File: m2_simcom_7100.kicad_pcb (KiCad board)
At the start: 2 copper layers, 42 x 30 mm, 5 parts, among them J1 M.2_Key_B

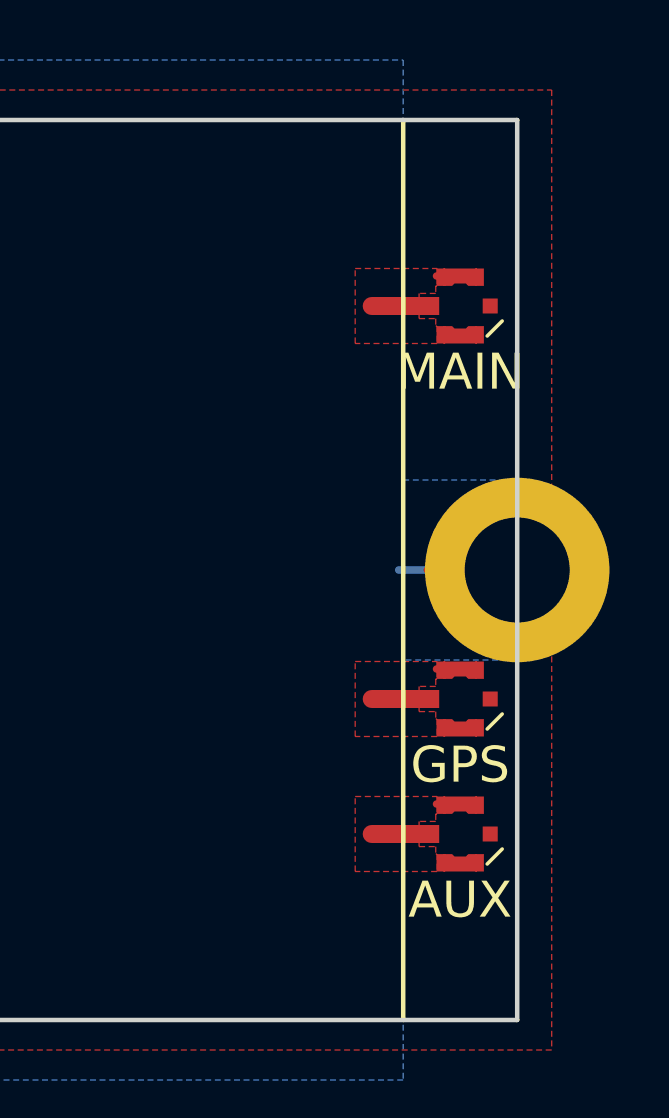
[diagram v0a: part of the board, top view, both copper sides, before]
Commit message: Fix footprint associations in netlist which are pointing to the wrong library name
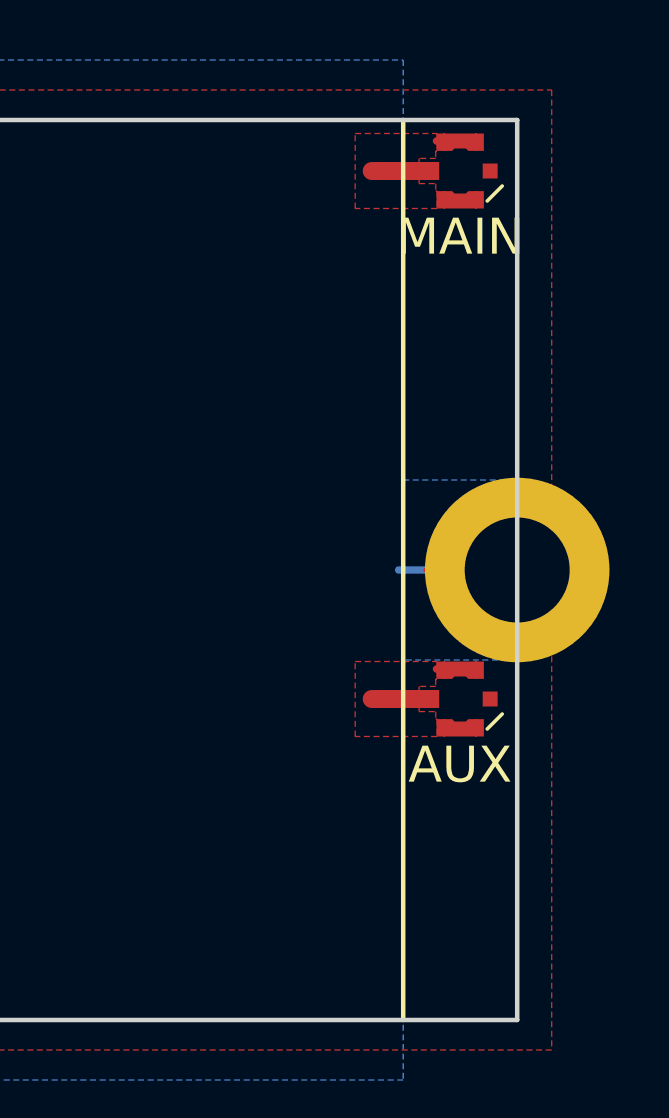
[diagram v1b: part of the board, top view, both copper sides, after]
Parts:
- removed ANT1: Conn_Coaxial, m2_key_b_3042:MHF4_20449-001E
- ANT2: footprint m2_key_b_3042:MHF4_20449-001E -> m2_simcom_7100:MHF4_20449-001E
- ANT5: renamed from ANT4; footprint m2_key_b_3042:MHF4_20449-001E -> m2_simcom_7100:MHF4_20449-001E
- J1: footprint m2_key_b_3042:M.2_Key_B_Gold_Fingers -> m2_simcom_7100:M.2_Key_B_Gold_Fingers
- moved ANT5 4.50 mm to (158.9, 81.7)
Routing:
- net /AUX: track 1.97 -> 0.00 mm
- net GND: track 31.9 -> 31.1 mm
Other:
- board text removed: "GPS"

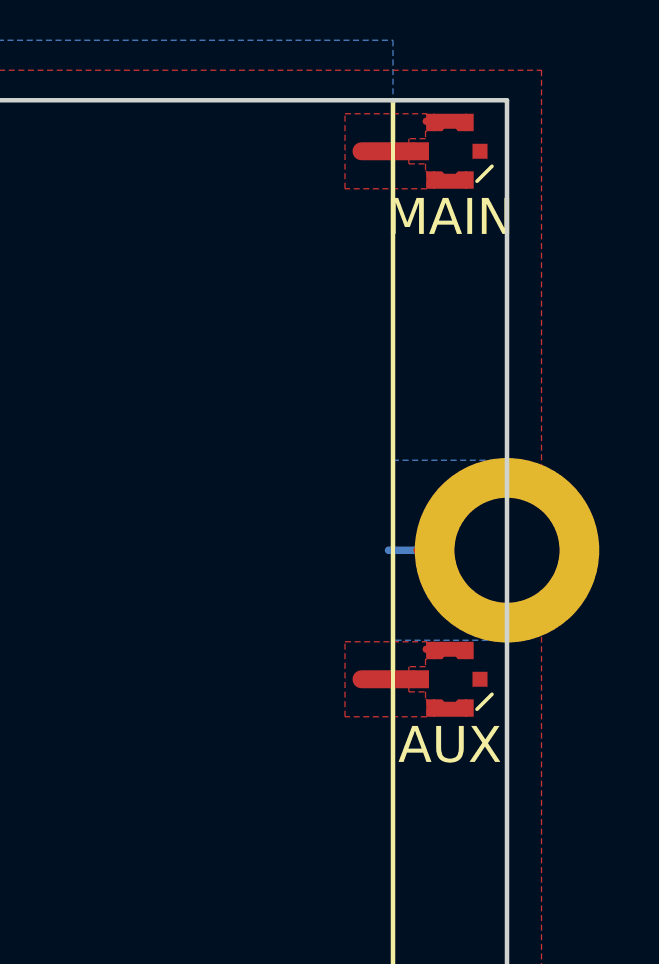
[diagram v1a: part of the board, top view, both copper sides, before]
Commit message: Swap Main and Div antenna positions
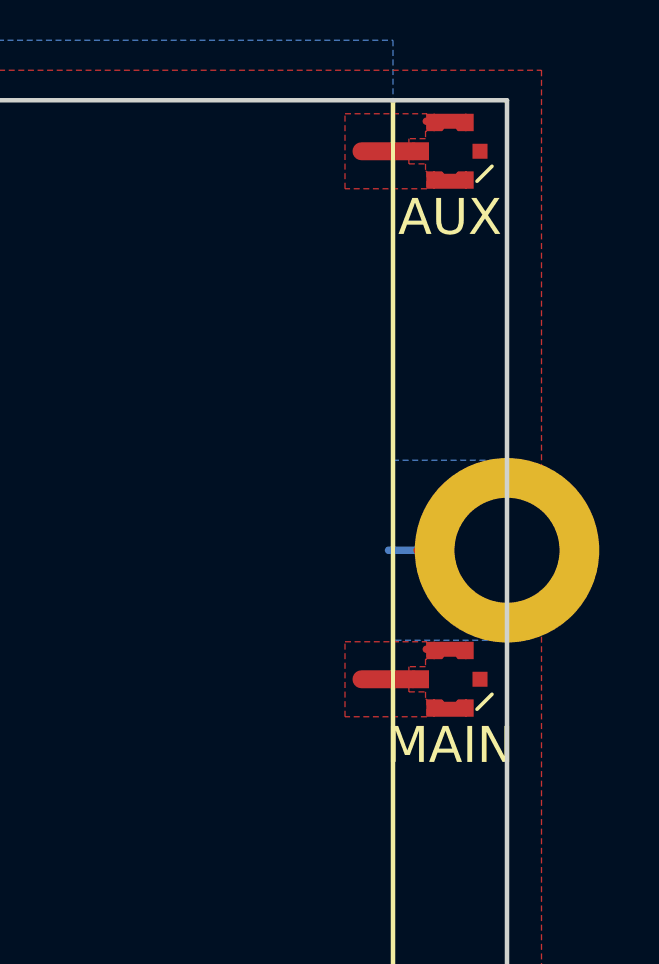
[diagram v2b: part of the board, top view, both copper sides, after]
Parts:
- ANT2: value Conn_Coaxial -> Main_Antenna
- ANT5: value Conn_Coaxial -> Div_Antenna
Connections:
- net +3V3 renamed VBAT
- net /DEVSLP renamed Net-(J1-Pad38)
- net /GPIO_0 renamed /HSIC_Data
- net /GPIO_1 renamed /HSIC_Strobe
- net /GPIO_10 renamed /UART_CTS
- net /GPIO_11 renamed /UART_RI/~WoWWAN
- net /GPIO_12 renamed /UART_RX
- net /GPIO_2 renamed /UART_DTR
- net /GPIO_3 renamed /UART_RTS
- net /GPIO_4 renamed /UART_DCD
- net /GPIO_5 renamed /PCM_CLK
- net /GPIO_6 renamed /PCM_IN
- net /GPIO_7 renamed /PCM_OUT
- net /GPIO_8 renamed /PCM_SYNC
- net /GPIO_9/DAS/~DSS renamed /UART_TX
- net /GPS renamed Net-(ANT2-Pad1)
- net /MAIN renamed Net-(ANT5-Pad1)
- net /PERn0/SATA-B+ renamed Net-(J1-Pad41)
- net /PERn1/USB3.0-Rx-/SSIC-RxN renamed /USB3.0-Tx-
- net /PERp0/SATA-B- renamed Net-(J1-Pad43)
- net /PERp1/USB3.0-Rx+/SSIC-RxP renamed /USB3.0-Tx+
- net /PETn0/SATA-A- renamed Net-(J1-Pad47)
- net /PETn1/USB3.0-Tx-/SSIC-TxN renamed /USB3.0-Rx-
- net /PETp0/SATA-A+ renamed Net-(J1-Pad49)
- net /PETp1/USB3.0-Tx+/SSIC-TxP renamed /USB3.0-Rx+
- net /REFCLKN renamed Net-(J1-Pad53)
- net /REFCLKP renamed Net-(J1-Pad55)
- net /~CLKREQ renamed Net-(J1-Pad52)
- net /~PERST renamed Net-(J1-Pad50)
- net /~PEWake renamed Net-(J1-Pad54)
- J1 pad 21: /CONFIG_0 -> GND

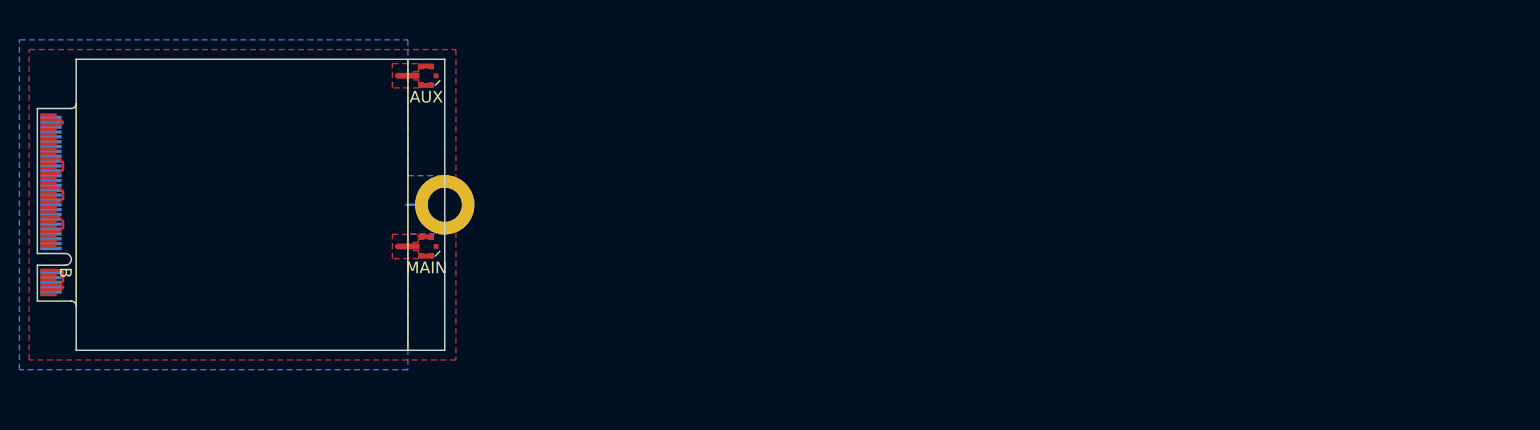
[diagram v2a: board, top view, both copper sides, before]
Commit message: Import the netlist and associated footprints into the layout
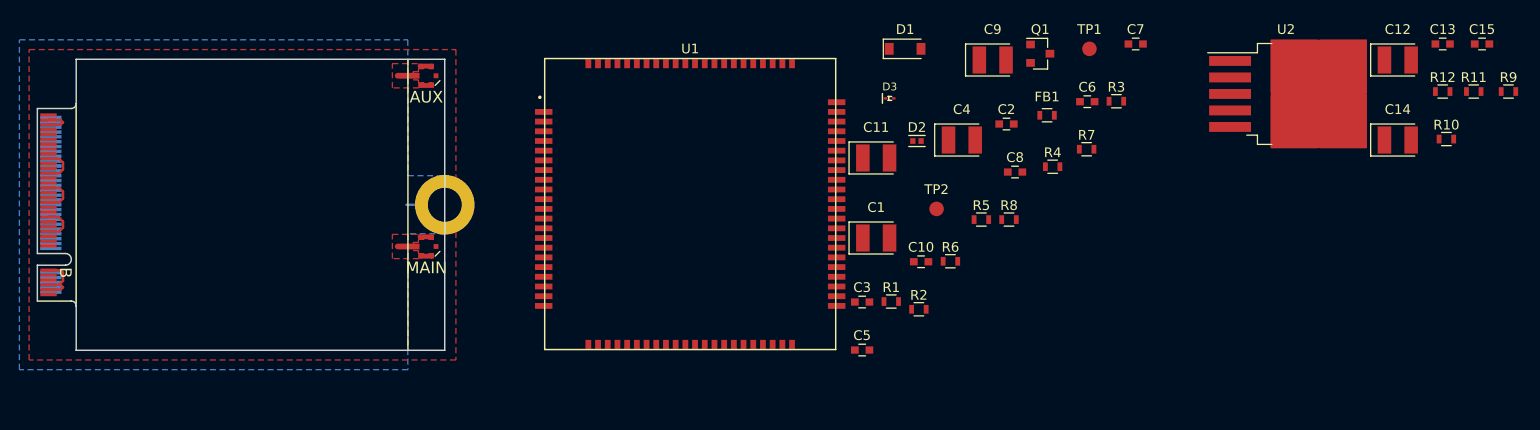
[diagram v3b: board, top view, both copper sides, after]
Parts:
- added C1: 100uF, m2_simcom_7100:CP_Tantalum_Case-B_EIA-3528-21_Reflow, F.Cu at (205.3, 98.4)
- added C10: NC, Capacitors_SMD:C_0603, F.Cu at (210.0, 100.9)
- added C11: 100uF, m2_simcom_7100:CP_Tantalum_Case-B_EIA-3528-21_Reflow, F.Cu at (205.3, 90.2)
- added C12: 100uF, m2_simcom_7100:CP_Tantalum_Case-B_EIA-3528-21_Reflow, F.Cu at (259.1, 80.1)
- added C13: 1uF, Capacitors_SMD:C_0603, F.Cu at (263.7, 78.4)
- added C14: 100uF, m2_simcom_7100:CP_Tantalum_Case-B_EIA-3528-21_Reflow, F.Cu at (259.1, 88.3)
- added C15: 100nF, Capacitors_SMD:C_0603, F.Cu at (267.8, 78.4)
- added C2: NC, Capacitors_SMD:C_0603, F.Cu at (218.8, 86.7)
- added C3: NC, Capacitors_SMD:C_0603, F.Cu at (203.9, 105.0)
- added C4: NC, m2_simcom_7100:CP_Tantalum_Case-B_EIA-3528-21_Reflow, F.Cu at (214.2, 88.3)
- added C5: 1uF, Capacitors_SMD:C_0603, F.Cu at (203.9, 110.0)
- added C6: NC, Capacitors_SMD:C_0603, F.Cu at (227.1, 84.4)
- added C7: NC, Capacitors_SMD:C_0603, F.Cu at (232.1, 78.4)
- added C8: 100nF, Capacitors_SMD:C_0603, F.Cu at (219.6, 91.6)
- added C9: 100uF, m2_simcom_7100:CP_Tantalum_Case-B_EIA-3528-21_Reflow, F.Cu at (217.3, 80.1)
- added D1: MMSZ5231BT1G, m2_simcom_7100:D_SOD-123, F.Cu at (208.3, 78.9)
- added D2: NC, m2_simcom_7100:D_0402, F.Cu at (209.5, 88.4)
- added D3: ESD9L5.0ST5G, m2_simcom_7100:D_SOD-923, F.Cu at (206.7, 84.0)
- added FB1: Ferrite, Inductors_SMD:L_0603, F.Cu at (222.9, 85.8)
- added Q1: NC, TO_SOT_Packages_SMD:SOT-23, F.Cu at (222.2, 79.4)
- added R1: NC, Resistors_SMD:R_0603, F.Cu at (206.9, 105.0)
- added R10: 100k, Resistors_SMD:R_0603, F.Cu at (264.1, 88.2)
- added R11: 47k, Resistors_SMD:R_0603, F.Cu at (266.9, 83.3)
- added R12: NC, Resistors_SMD:R_0603, F.Cu at (263.7, 83.3)
- added R2: NC, Resistors_SMD:R_0603, F.Cu at (209.7, 105.8)
- added R3: 0, Resistors_SMD:R_0603, F.Cu at (230.1, 84.3)
- added R4: 51, Resistors_SMD:R_0603, F.Cu at (223.5, 91.1)
- added R5: 51, Resistors_SMD:R_0603, F.Cu at (216.2, 96.5)
- added R6: 51, Resistors_SMD:R_0603, F.Cu at (213.0, 100.8)
- added R7: 10k, Resistors_SMD:R_0603, F.Cu at (227.0, 89.3)
- added R8: 0, Resistors_SMD:R_0603, F.Cu at (219.0, 96.5)
- added R9: 100k, Resistors_SMD:R_0603, F.Cu at (270.5, 83.3)
- added TP1: TEST_1P, Measurement_Points:Measurement_Point_Round-SMD-Pad_Small, F.Cu at (227.3, 78.9)
- added TP2: TEST_1P, Measurement_Points:Measurement_Point_Round-SMD-Pad_Small, F.Cu at (211.5, 95.4)
- added U1: SIM7100, m2_simcom_7100:SIMCom_7100, F.Cu at (186.2, 94.9)
- added U2: MIC29302, m2_simcom_7100:TO-263-5_TabPin6, F.Cu at (247.6, 83.6)

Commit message: Swapping out the MIC29302 4.46mm thick TO-263 LDO with the smaller RT9059 WDFN-10L part which can handle the high current transients in a much more suitable package
The package is also much cheaper!
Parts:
- moved C7 76.6 mm to (156.0, 87.0), turned to 270 degrees
- moved R3 76.4 mm to (156.0, 103.0), turned to 270 degrees
- moved C6 74.3 mm to (156.0, 106.0), turned to 270 degrees
- moved R8 64.2 mm to (156.0, 84.1), turned to 90 degrees
- moved C10 58.1 mm to (155.0, 82.0), turned to 180 degrees
- moved C3 48.3 mm to (156.0, 99.0), turned to 90 degrees
- moved U1 48.2 mm to (138.0, 95.0)
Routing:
- net Net-(C6-Pad1): track 0.00 -> 4.50 mm
- net Net-(ANT2-Pad1): track 1.97 -> 4.94 mm
- net Net-(C7-Pad1): track 0.00 -> 1.40 mm
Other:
- board text added: "Figure 3 Describes Stack Up Dimensions"

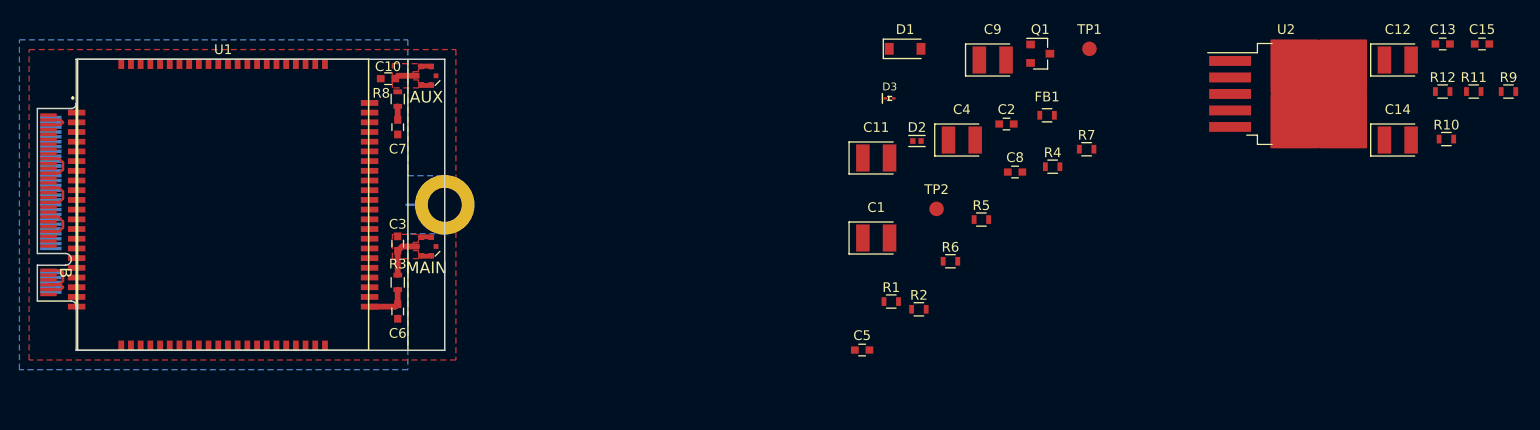
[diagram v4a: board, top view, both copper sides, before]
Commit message: Use the RT9059 LDO in the layout instead of the old MIC29302 one
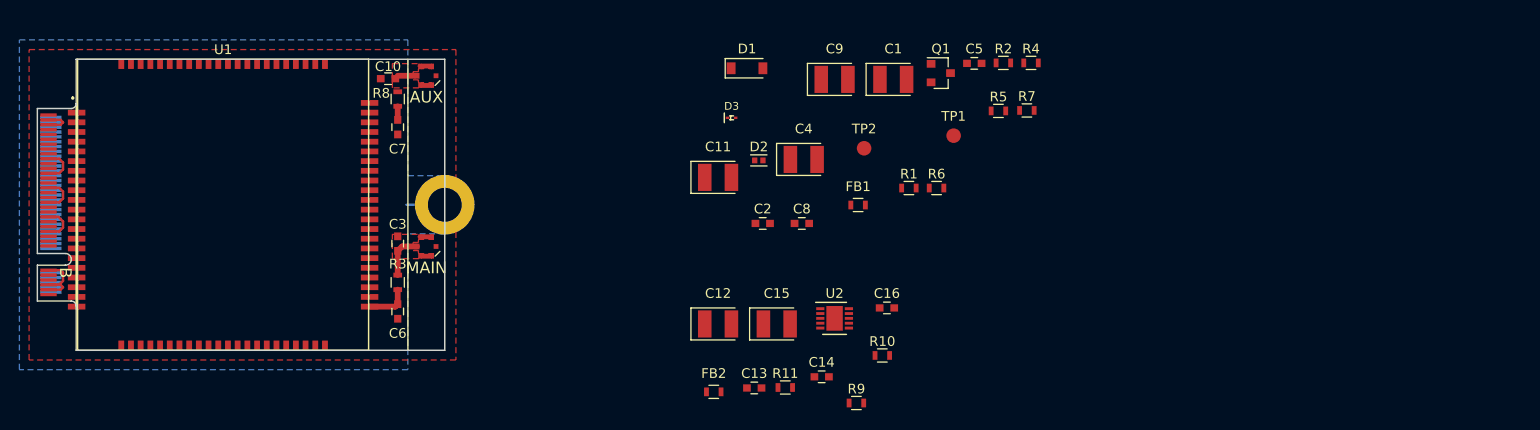
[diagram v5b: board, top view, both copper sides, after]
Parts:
- removed R12: NC, Resistors_SMD:R_0603
- added C16: 100nF, Capacitors_SMD:C_0603, F.Cu at (206.4, 105.6)
- added FB2: Ferrite, Inductors_SMD:L_0603, F.Cu at (188.6, 114.3)
- C14: value 100uF -> 1uF; footprint m2_simcom_7100:CP_Tantalum_Case-B_EIA-3528-21_Reflow -> Capacitors_SMD:C_0603
- C15: value 100nF -> 100uF; footprint Capacitors_SMD:C_0603 -> m2_simcom_7100:CP_Tantalum_Case-B_EIA-3528-21_Reflow
- R10: value 100k -> 180k
- U2: value MIC29302 -> RT9059; footprint m2_simcom_7100:TO-263-5_TabPin6 -> m2_simcom_7100:DFN-10-1EP_3x3mm_Pitch0.5mm
- moved C13 79.3 mm to (192.8, 113.9)
- moved C15 78.2 mm to (195.1, 107.3)
- moved R11 77.3 mm to (196.0, 113.8)
- moved C12 75.2 mm to (189.0, 107.3)
- moved R9 74.5 mm to (203.3, 115.4)
- moved C14 64.2 mm to (199.7, 112.7)
- moved R10 62.3 mm to (206.0, 110.5)
- moved U2 52.0 mm to (201.0, 106.7)
- moved C5 31.7 mm to (215.4, 80.4)
- moved C2 27.1 mm to (193.6, 96.9)
- moved R2 26.9 mm to (218.4, 80.4)
- moved C8 22.6 mm to (197.7, 96.9)
- moved FB1 21.6 mm to (203.5, 95.0)
- moved TP1 16.6 mm to (213.3, 87.9)
- moved C1 16.4 mm to (207.1, 82.1)
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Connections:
- net Net-(ANT2-Pad1) renamed /MAIN
- net Net-(ANT5-Pad1) renamed /AUX
- C14 pad 1: VBAT_REG -> Net-(C14-Pad1)
- R9 pad 1: /~Full_Card_Power_Off -> VBAT_REG
- R9 pad 2: GND -> Net-(R9-Pad2)
- U2 pad 1: /~Full_Card_Power_Off -> VBAT_REG
- U2 pad 2: VBAT -> VBAT_REG
- U2 pad 3: GND -> VBAT_REG
- U2 pad 4: VBAT_REG -> Net-(R10-Pad2)
- U2 pad 5: Net-(R10-Pad2) -> Net-(R9-Pad2)
- U2 pad 6: GND -> /~Full_Card_Power_Off
